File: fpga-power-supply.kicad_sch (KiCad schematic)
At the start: 69 parts, among them U21 ECP5UM5G_85_CABGA756

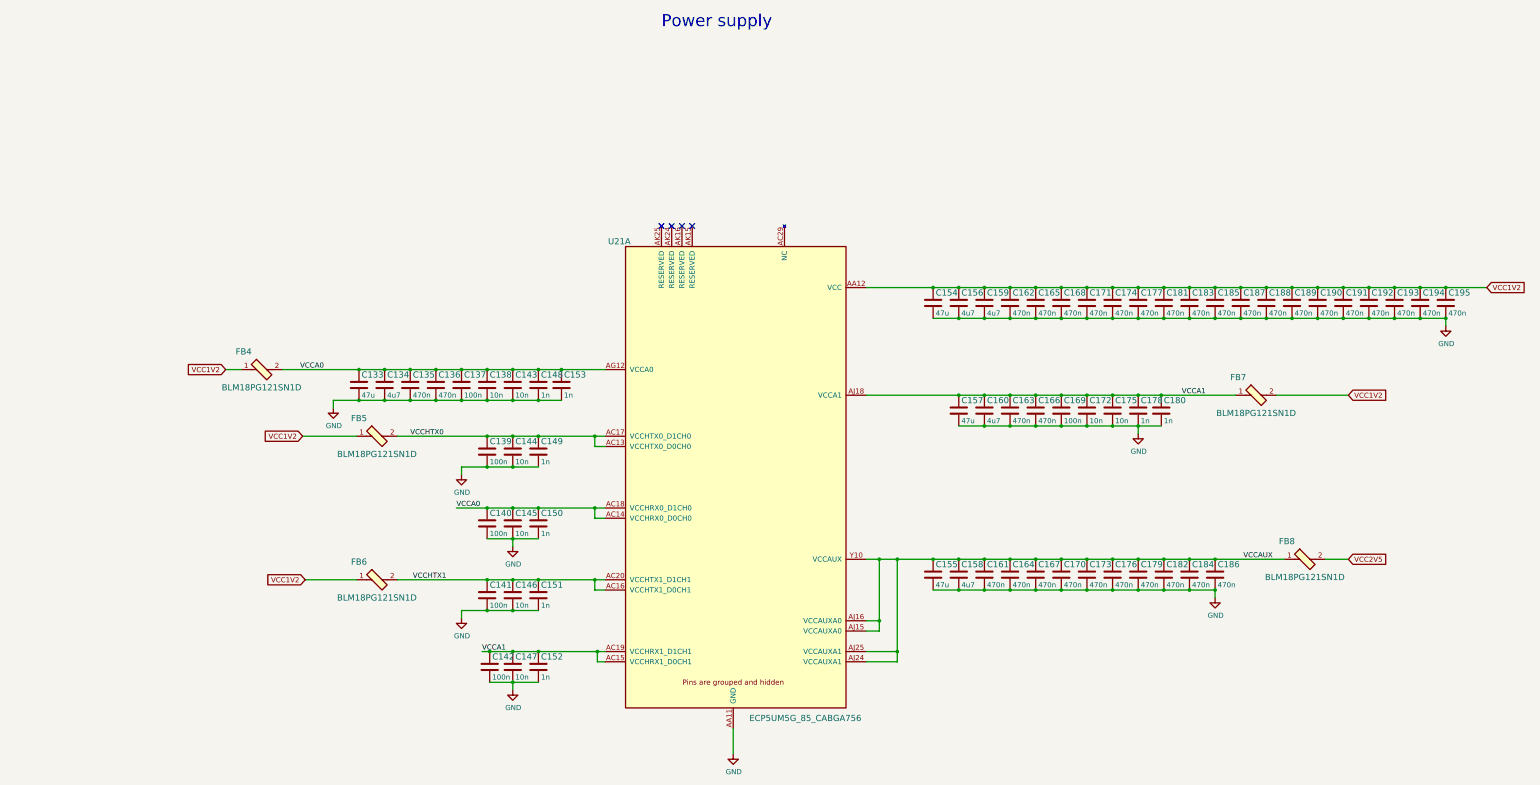
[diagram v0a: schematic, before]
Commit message: [#61392] Convert project to KiCad 7
[#61392] Run globlib

[#61392] Allign components to the grid

[#61392] Update oshw and antmicro logo

[#61392] Standarize ethernet sheet

[#61392] Standarize pcie-conn sheet

[#61392] Standarize rot sheet

[#61392] Standarize edge-connector sheet

[#61392] WIP:Standarize interfaces sheet

[#61392] WIP: Route interfaces sheet

[#61392] Finish standarizing interfaces sheet

[#61392] Update interfaces sheet with fixed 2N7002

[#61392] WIP:Standarize ddr3 sheet

[#61392] Standarize ddr3 sheet

[#61392] Standarize power-supply sheet

[#61392] Standarize fpga power-supply sheet

[#61392] Remove TODO comments from power-banks sheet

[#61392] Standarize fpga-banks sheet

[#61392] Ignore Input pins not driven ERC

[#61392] Clear off grid ERCs

[#61392] Exclude ERC DDR3_VTT_EN NC

[#61392] Bump rev to 1.2.1

[#61392] Bump PCB rev to 1.2.1
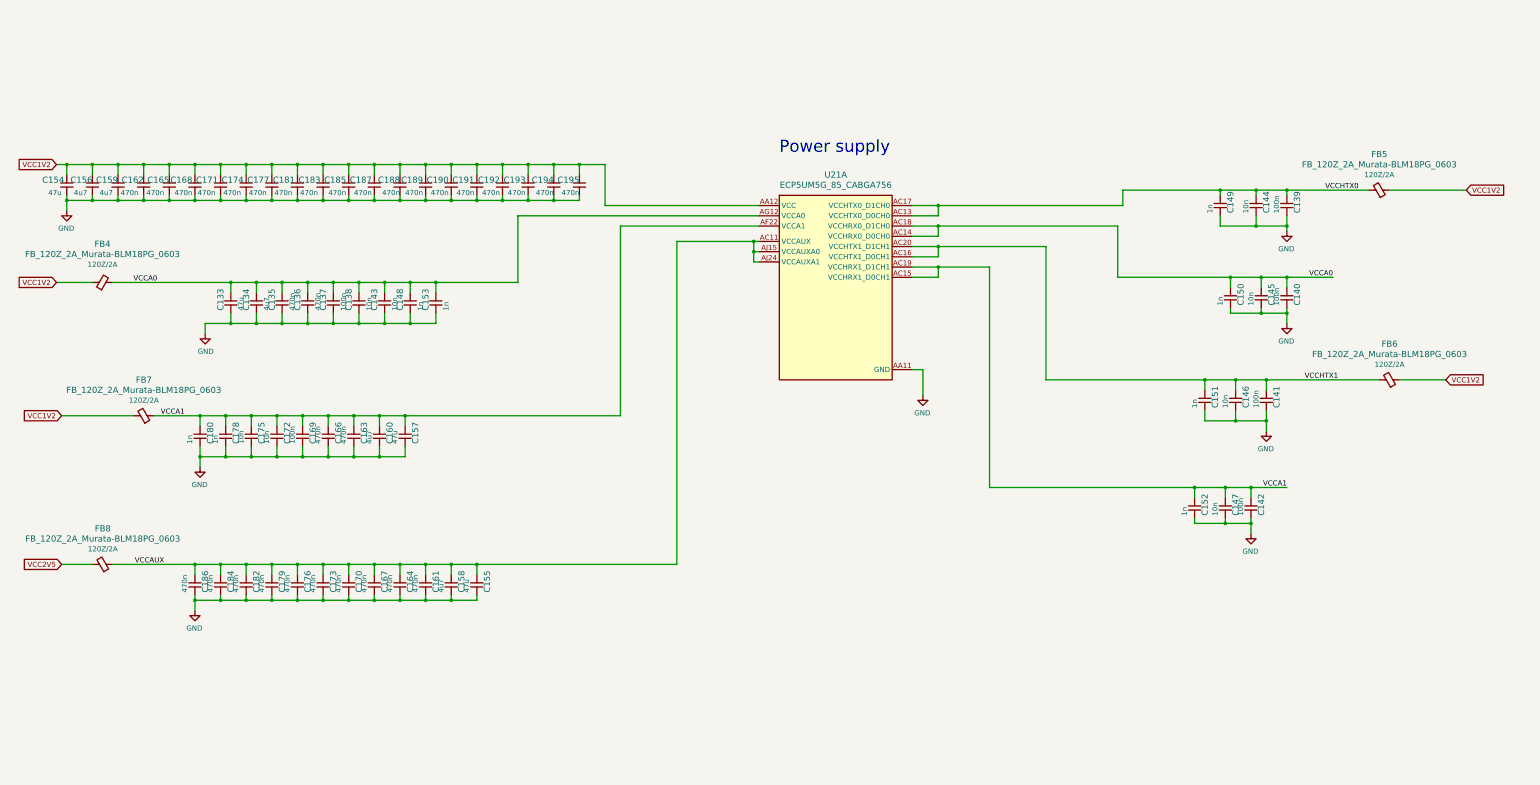
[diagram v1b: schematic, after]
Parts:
- C133, C154, C155, C157: footprint ecp5-dc-scm-footprints:0603-cap -> antmicro-footprints:C_0603_1608Metric; symbol ecp5-dc-scm:C_47u_0603 -> antmicroCapacitors0603:C_47u_0603; Author (none) -> Antmicro; License (none) -> Apache-2.0; Manufacturer MURATA -> Murata; Public (none) -> False
- C134, C156, C158, C159, C160: footprint ecp5-dc-scm-footprints:0402-cap -> antmicro-footprints:C_0402_1005Metric; symbol ecp5-dc-scm:C_4u7_0402 -> antmicroCapacitors0402:C_4u7_0402; Author (none) -> Antmicro; License (none) -> Apache-2.0; Manufacturer MURATA -> Murata; Public (none) -> False
- C135, C136, C161, C162, C163, C164, C165, C166, C167, C168, C170, C171, C173, C174, C176, C177, C179, C181, C182, C183, C184, C185, C186, C187, C188, C189, C190, C191, C192, C193, C194, C195: footprint ecp5-dc-scm-footprints:0402-cap -> antmicro-footprints:C_0402_1005Metric; symbol ecp5-dc-scm:C_470n_0402 -> antmicroCapacitors0402:C_470n_0402; Author (none) -> Antmicro; License (none) -> Apache-2.0; Public (none) -> False
- C137, C139, C140, C141, C142, C169: footprint ecp5-dc-scm-footprints:0402-cap -> antmicro-footprints:C_0402_1005Metric; symbol ecp5-dc-scm:C_100n_0402 -> antmicroCapacitors0402:C_100n_0402; Author (none) -> Antmicro; Dielectric (none) -> X5R; License (none) -> Apache-2.0; MPN 0402X104K6R3CT -> GRM155R61H104KE14D; Manufacturer Walsin -> Murata; Public (none) -> False; Voltage (none) -> 50V
- C138, C143, C144, C145, C146, C147, C172, C175: footprint ecp5-dc-scm-footprints:0402-cap -> antmicro-footprints:C_0402_1005Metric; symbol ecp5-dc-scm:C_10n_0402 -> antmicroCapacitors0402:C_10n_0402; Author (none) -> Antmicro; Dielectric (none) -> X7R; License (none) -> Apache-2.0; MPN 04025G103ZAT2A -> GRM155R71H103KA88D; Manufacturer AVX -> Murata; Public (none) -> False; Voltage (none) -> 50V
- C148, C149, C150, C151, C152, C153, C178, C180: footprint ecp5-dc-scm-footprints:0402-res -> antmicro-footprints:C_0402_1005Metric; symbol ecp5-dc-scm:C_1n_0402 -> antmicroCapacitors0402:C_1n_0402; Author (none) -> Antmicro; Dielectric (none) -> C0G; License (none) -> Apache-2.0; MPN CC0402KRX7R9BB102 -> GRM1555C1H102JA01D; Manufacturer YAGEO -> Murata; Public (none) -> False; Voltage (none) -> 50V
- FB4, FB5, FB6, FB7, FB8: value BLM18PG121SN1D -> FB_120Z_2A_Murata-BLM18PG_0603; footprint ecp5-dc-scm-footprints:0603-res -> antmicro-footprints:FB_0603_1608Metric; symbol ecp5-dc-scm:BLM18PG121SN1D -> antmicroFerriteBeadsandChips:FB_120Z_2A_Murata-BLM18PG_0603; Author (none) -> Antmicro; License (none) -> Apache-2.0; Manufacturer Murata Electronics North America -> Murata; Public (none) -> False; Val (none) -> 120Z/2A
- U21: footprint ecp5-dc-scm-footprints:CABGA756_27x27mm_p0.8mm -> antmicro-footprints:BGA-1024-756_27x27mm_Layout32x32_P0.8mm; symbol ecp5-dc-scm:ECP5UM5G_85_CABGA756-ecp5-dc-scm -> antmicroFPGAChips:ECP5_LFE5UM5G-85; Author (none) -> Antmicro; License (none) -> Apache-2.0
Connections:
- net GND: now also C133.1, C134.1, C135.1, C136.1, C137.1, C138.1, C139.1, C140.1, C141.1, C142.1, C143.1, C144.1, C145.1, C146.1, C147.1, C148.1, C149.1, C150.1, C151.1, C152.1, C153.1, C155.1, C157.1, C158.1, C160.1, C161.1, C163.1, C164.1, C166.1, C167.1, C169.1, C170.1, C172.1, C173.1, C175.1, C176.1, C178.1, C179.1, C180.1, C182.1, C184.1, C186.1; no longer C133.2, C134.2, C135.2, C136.2, C137.2, C138.2, C139.2, C140.2, C141.2, C142.2, C143.2, C144.2, C145.2, C146.2, C147.2, C148.2, C149.2, C150.2, C151.2, C152.2, C153.2, C155.2, C157.2, C158.2, C160.2, C161.2, C163.2, C164.2, C166.2, C167.2, C169.2, C170.2, C172.2, C173.2, C175.2, C176.2, C178.2, C179.2, C180.2, C182.2, C184.2, C186.2
- net VCCA0: now also C133.2, C134.2, C135.2, C136.2, C137.2, C138.2, C140.2, C143.2, C145.2, C148.2, C150.2, C153.2; no longer C133.1, C134.1, C135.1, C136.1, C137.1, C138.1, C140.1, C143.1, C145.1, C148.1, C150.1, C153.1
- net VCCA1: now also C142.2, C147.2, C152.2, C157.2, C160.2, C163.2, C166.2, C169.2, C172.2, C175.2, C178.2, C180.2; no longer C142.1, C147.1, C152.1, C157.1, C160.1, C163.1, C166.1, C169.1, C172.1, C175.1, C178.1, C180.1
- net VCCAUX: now also C155.2, C158.2, C161.2, C164.2, C167.2, C170.2, C173.2, C176.2, C179.2, C182.2, C184.2, C186.2; no longer C155.1, C158.1, C161.1, C164.1, C167.1, C170.1, C173.1, C176.1, C179.1, C182.1, C184.1, C186.1
- net VCCHTX0: now also C139.2, C144.2, C149.2; no longer C139.1, C144.1, C149.1
- net VCCHTX1: now also C141.2, C146.2, C151.2; no longer C141.1, C146.1, C151.1
- net VCC renamed VCC1V2
- no-connect marks 4 -> 0
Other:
- moved on the sheet: C133, C134, C135, C136, C137, C138, C139, C140, C141, C142, C143, C144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

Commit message: [#61392] Import changes to the PCB
[#61392] Fix D2 orientation

[#61392] Fix J2 J1 D6 orientation

[#61392] WIP: PCB Fix caps orienations

[#61392] PCB Fix caps orienations

[#61392] Fix missalligned edge cuts

[#61392] Sync Sch with PCB

[#61392] Fix silk clipped by edge cuts

[#61392] Ignore TP no courtyard drc

[#61392] Update C_0603 footprints

[#61392] Update R_0402 footprints

[#61392] Update Sot-23 footprints

[#61392] Update QFN and IHLP footprints

[#61392] Update remaining footprints

[#61392] Change minimal text height to 0.7mm

[#61392] Clear remaining Silk DRCs

[#61392] Update TPS51200DRCT symbol

[#61392] Update 9774040151

[#61392] Update W25Q32JVS

[#61392] Update ECS-3225MVQ-1000CN-TR

[#61392] Clean ERC

[#61392] Remove obsolete files

[#61392] Synhronize components with library

[#61392] Remove globlib leftovers

[#61392] Synchronize components with libraries (WiP)

[#61392] Clean ERC and DRC

[#61392] Set J5 to DNP

[#61392] Add PCB SHA string, update layer names

[#61392] Update assets

[#62567] Add stackup.csv

[#62567] Input elecric constants for the board stackup

[#62567] Update stackup.csv
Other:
- moved on the sheet: C153
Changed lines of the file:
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@@
   (title_block
     (title "ECP5 - Datacenter Secure Control Module (DC-SCM)")
-    (date "2024-07-01")
+    (date "2024-07-15")
     (rev "1.2.1")
   )
@@
     (stroke (width 0) (type default))
   )
+  (wire (pts (xy 62.23 163.83) (xy 62.23 165.1))
+    (stroke (width 0) (type default))
+  )
   (wire (pts (xy 100.33 165.1) (xy 93.98 165.1))
     (stroke (width 0) (type default))
@@
     (stroke (width 0) (type default))
   )
+  (wire (pts (xy 323.85 144.78) (xy 323.85 146.05))
+    (stroke (width 0) (type default))
+  )
   (wire (pts (xy 246.38 83.82) (xy 246.38 81.28))
     (stroke (width 0) (type default))
@@
     (stroke (width 0) (type default))
   )
+  (wire (pts (xy 332.74 92.71) (xy 332.74 93.98))
+    (stroke (width 0) (type default))
+  )
   (wire (pts (xy 201.93 87.63) (xy 200.66 87.63))
     (stroke (width 0) (type default))
@@
     (stroke (width 0) (type default))
   )
+  (wire (pts (xy 327.66 118.11) (xy 327.66 119.38))
+    (stroke (width 0) (type default))
+  )
   (wire (pts (xy 326.39 101.6) (xy 326.39 102.87))
     (stroke (width 0) (type default))
@@
     (stroke (width 0) (type default))
   )
+  (wire (pts (xy 332.74 71.12) (xy 332.74 72.39))
+    (stroke (width 0) (type default))
+  )
   (wire (pts (xy 163.83 66.04) (xy 163.83 76.2))
     (stroke (width 0) (type default))
@@
     )
   )
-  (symbol (lib_id "antmicroCapacitors0402:C_1n_0402") (at 121.92 102.87 90) (unit 1)
+  (symbol (lib_id "antmicroCapacitors0402:C_1n_0402") (at 121.92 102.87 270) (mirror x) (unit 1)
     (in_bom yes) (on_board yes) (dnp no)
-    (property "Reference" "C153" (at 119.38 102.235 0)
+    (property "Reference" "C153" (at 124.46 102.235 0)
       (effects (font (size 1.524 1.524)) (justify left))
     )
-    (property "Value" "C_1n_0402" (at 125.73 102.87 0)
+    (property "Value" "C_1n_0402" (at 118.11 102.87 0)
       (effects (font (size 1.524 1.524)) hide)
     )
-    (property "Footprint" "antmicro-footprints:C_0402_1005Metric" (at 116.84 97.79 0)
+    (property "Footprint" "antmicro-footprints:C_0402_1005Metric" (at 127 97.79 0)
       (effects (font (size 1.524 1.524)) (justify left) hide)
     )
@@
       (effects (font (size 1.27 1.27)) hide)
     )
-    (property "Manufacturer" "Murata" (at 111.76 97.79 0)
+    (property "Manufacturer" "Murata" (at 132.08 97.79 0)
       (effects (font (size 1.524 1.524)) (justify left) hide)
     )
-    (property "MPN" "GRM1555C1H102JA01D" (at 114.3 97.79 0)
+    (property "MPN" "GRM1555C1H102JA01D" (at 129.54 97.79 0)
       (effects (font (size 1.524 1.524)) (justify left) hide)
     )
-    (property "Val" "1n" (at 124.46 102.235 0)
+    (property "Val" "1n" (at 119.38 102.235 0)
       (effects (font (size 1.27 1.27)) (justify left))
     )
-    (property "License" "Apache-2.0" (at 144.78 82.55 0)
+    (property "License" "Apache-2.0" (at 99.06 82.55 0)
       (effects (font (size 1.27 1.27) (thickness 0.15)) (justify left bottom) hide)
     )
-    (property "Author" "Antmicro" (at 147.32 82.55 0)
+    (property "Author" "Antmicro" (at 96.52 82.55 0)
       (effects (font (size 1.27 1.27) (thickness 0.15)) (justify left bottom) hide)
     )
-    (property "Voltage" "50V" (at 149.86 82.55 0)
+    (property "Voltage" "50V" (at 93.98 82.55 0)
       (effects (font (size 1.27 1.27)) (justify left bottom) hide)
     )
-    (property "Dielectric" "C0G" (at 152.4 82.55 0)
+    (property "Dielectric" "C0G" (at 91.44 82.55 0)
       (effects (font (size 1.27 1.27)) (justify left bottom) hide)
     )
-    (property "Public" "False" (at 154.94 82.55 0)
+    (property "Public" "False" (at 88.9 82.55 0)
       (effects (font (size 1.27 1.27)) (justify left bottom) hide)
     )
@@
     )
   )
+  (symbol (lib_id "antmicropower:PWR_FLAG") (at 323.85 144.78 0) (unit 1)
+    (in_bom yes) (on_board yes) (dnp no)
+    (property "Reference" "#FLG010" (at 323.85 142.875 0)
+      (effects (font (size 1.27 1.27)) hide)
+    )
+    (property "Value" "PWR_FLAG" (at 323.85 140.97 0)
+      (effects (font (size 1.27 1.27)))
+    )
+    (property "Footprint" "" (at 323.85 144.78 0)
+      (effects (font (size 1.27 1.27)) hide)
+    )
+    (property "Datasheet" "" (at 323.85 144.78 0)
+      (effects (font (size 1.27 1.27)) hide)
+    )
+    (pin "1")
+    (instances
+      (project "ecp5-dc-scm"
+        (path "/809f9032-4d0f-476d-a3f0-9455af02883a/00000000-0000-0000-0000-00005fd86c51"
+          (reference "#FLG010") (unit 1)
+        )
+      )
+    )
+  )
+  (symbol (lib_id "antmicropower:PWR_FLAG") (at 332.74 92.71 0) (unit 1)
+    (in_bom yes) (on_board yes) (dnp no)
+    (property "Reference" "#FLG08" (at 332.74 90.805 0)
+      (effects (font (size 1.27 1.27)) hide)
+    )
+    (property "Value" "PWR_FLAG" (at 332.74 88.9 0)
+      (effects (font (size 1.27 1.27)))
+    )
+    (property "Footprint" "" (at 332.74 92.71 0)
+      (effects (font (size 1.27 1.27)) hide)
+    )
+    (property "Datasheet" "" (at 332.74 92.71 0)
+      (effects (font (size 1.27 1.27)) hide)
+    )
+    (pin "1")
+    (instances
+      (project "ecp5-dc-scm"
+        (path "/809f9032-4d0f-476d-a3f0-9455af02883a/00000000-0000-0000-0000-00005fd86c51"
+          (reference "#FLG08") (unit 1)
+        )
+      )
+    )
+  )
+  (symbol (lib_id "antmicropower:PWR_FLAG") (at 332.74 71.12 0) (unit 1)
+    (in_bom yes) (on_board yes) (dnp no)
+    (property "Reference" "#FLG07" (at 332.74 69.215 0)
+      (effects (font (size 1.27 1.27)) hide)
+    )
+    (property "Value" "PWR_FLAG" (at 327.66 67.31 0)
+      (effects (font (size 1.27 1.27)))
+    )
+    (property "Footprint" "" (at 332.74 71.12 0)
+      (effects (font (size 1.27 1.27)) hide)
+    )
+    (property "Datasheet" "" (at 332.74 71.12 0)
+      (effects (font (size 1.27 1.27)) hide)
+    )
+    (pin "1")
+    (instances
+      (project "ecp5-dc-scm"
+        (path "/809f9032-4d0f-476d-a3f0-9455af02883a/00000000-0000-0000-0000-00005fd86c51"
+          (reference "#FLG07") (unit 1)
+        )
+      )
+    )
+  )
   (symbol (lib_id "antmicropower:GND") (at 242.57 123.19 0) (mirror y) (unit 1)
     (in_bom yes) (on_board yes) (dnp no)
@@
         )
       )
+    )
+  )
+  (symbol (lib_id "antmicropower:PWR_FLAG") (at 62.23 163.83 0) (unit 1)
+    (in_bom yes) (on_board yes) (dnp no)
+    (property "Reference" "#FLG06" (at 62.23 161.925 0)
+      (effects (font (size 1.27 1.27)) hide)
+    )
+    (property "Value" "PWR_FLAG" (at 67.31 160.02 0)
+      (effects (font (size 1.27 1.27)))
+    )
+    (property "Footprint" "" (at 62.23 163.83 0)
+      (effects (font (size 1.27 1.27)) hide)
+    )
+    (property "Datasheet" "" (at 62.23 163.83 0)
+      (effects (font (size 1.27 1.27)) hide)
+    )
+    (pin "1")
+    (instances
+      (project "ecp5-dc-scm"
+        (path "/809f9032-4d0f-476d-a3f0-9455af02883a/00000000-0000-0000-0000-00005fd86c51"
+          (reference "#FLG06") (unit 1)
+        )
+      )
+    )
+  )
+  (symbol (lib_id "antmicropower:PWR_FLAG") (at 327.66 118.11 0) (unit 1)
+    (in_bom yes) (on_board yes) (dnp no)
+    (property "Reference" "#FLG09" (at 327.66 116.205 0)
+      (effects (font (size 1.27 1.27)) hide)
+    )
+    (property "Value" "PWR_FLAG" (at 327.66 114.3 0)
+      (effects (font (size 1.27 1.27)))
+    )
+    (property "Footprint" "" (at 327.66 118.11 0)
+      (effects (font (size 1.27 1.27)) hide)
+    )
+    (property "Datasheet" "" (at 327.66 118.11 0)
+      (effects (font (size 1.27 1.27)) hide)
+    )
+    (pin "1")
+    (instances
+      (project "ecp5-dc-scm"
+        (path "/809f9032-4d0f-476d-a3f0-9455af02883a/00000000-0000-0000-0000-00005fd86c51"
+          (reference "#FLG09") (unit 1)
+        )
+      )
